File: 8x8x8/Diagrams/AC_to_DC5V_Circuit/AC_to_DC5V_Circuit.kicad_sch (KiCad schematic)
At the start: 30 parts, among them J1 Conn_01x01 (Arduino Signal Pi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, J10 Conn_01x01 (Q3 +5V), J11 Conn_01x01 (Q3 -5V), J12 Conn_01x01 (Q4 +5V), J13 Conn_01x01 (Q4 -5V), J2 Conn_01x03, J3 Conn_01x01 (Arduino ground), J4 Conn_01x03, J6 Conn_01x01 (Q1 +5V), J7 Conn_01x01 (Q1 -5V)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

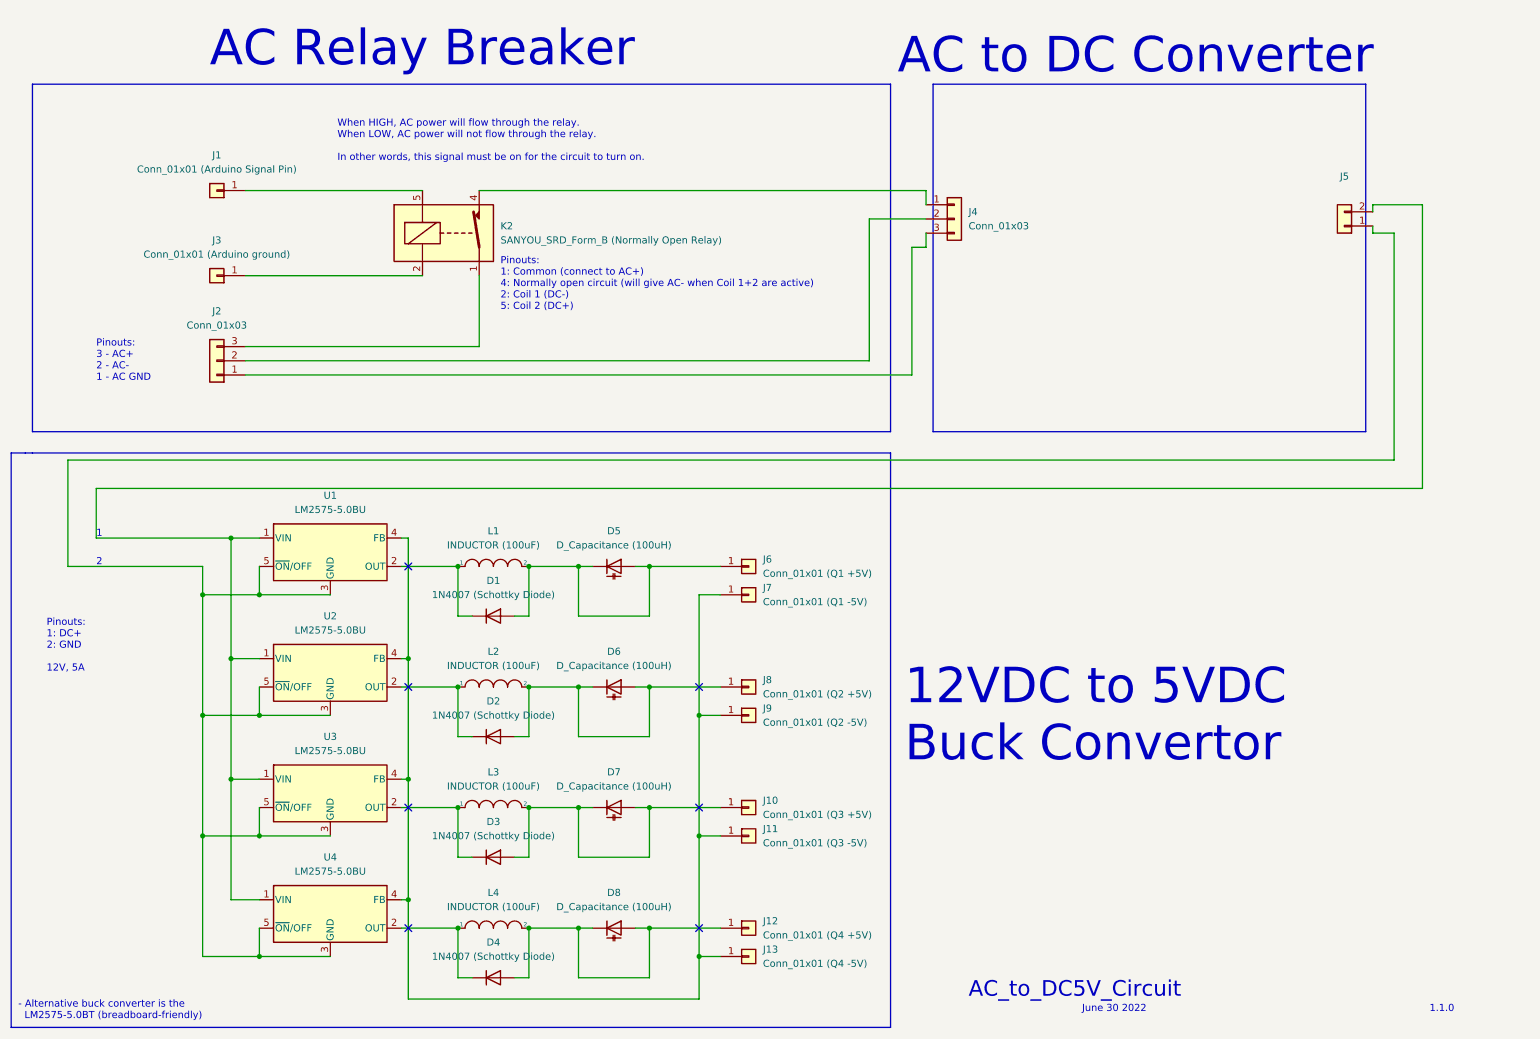
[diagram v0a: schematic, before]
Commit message: start AC->5VDC Circuit
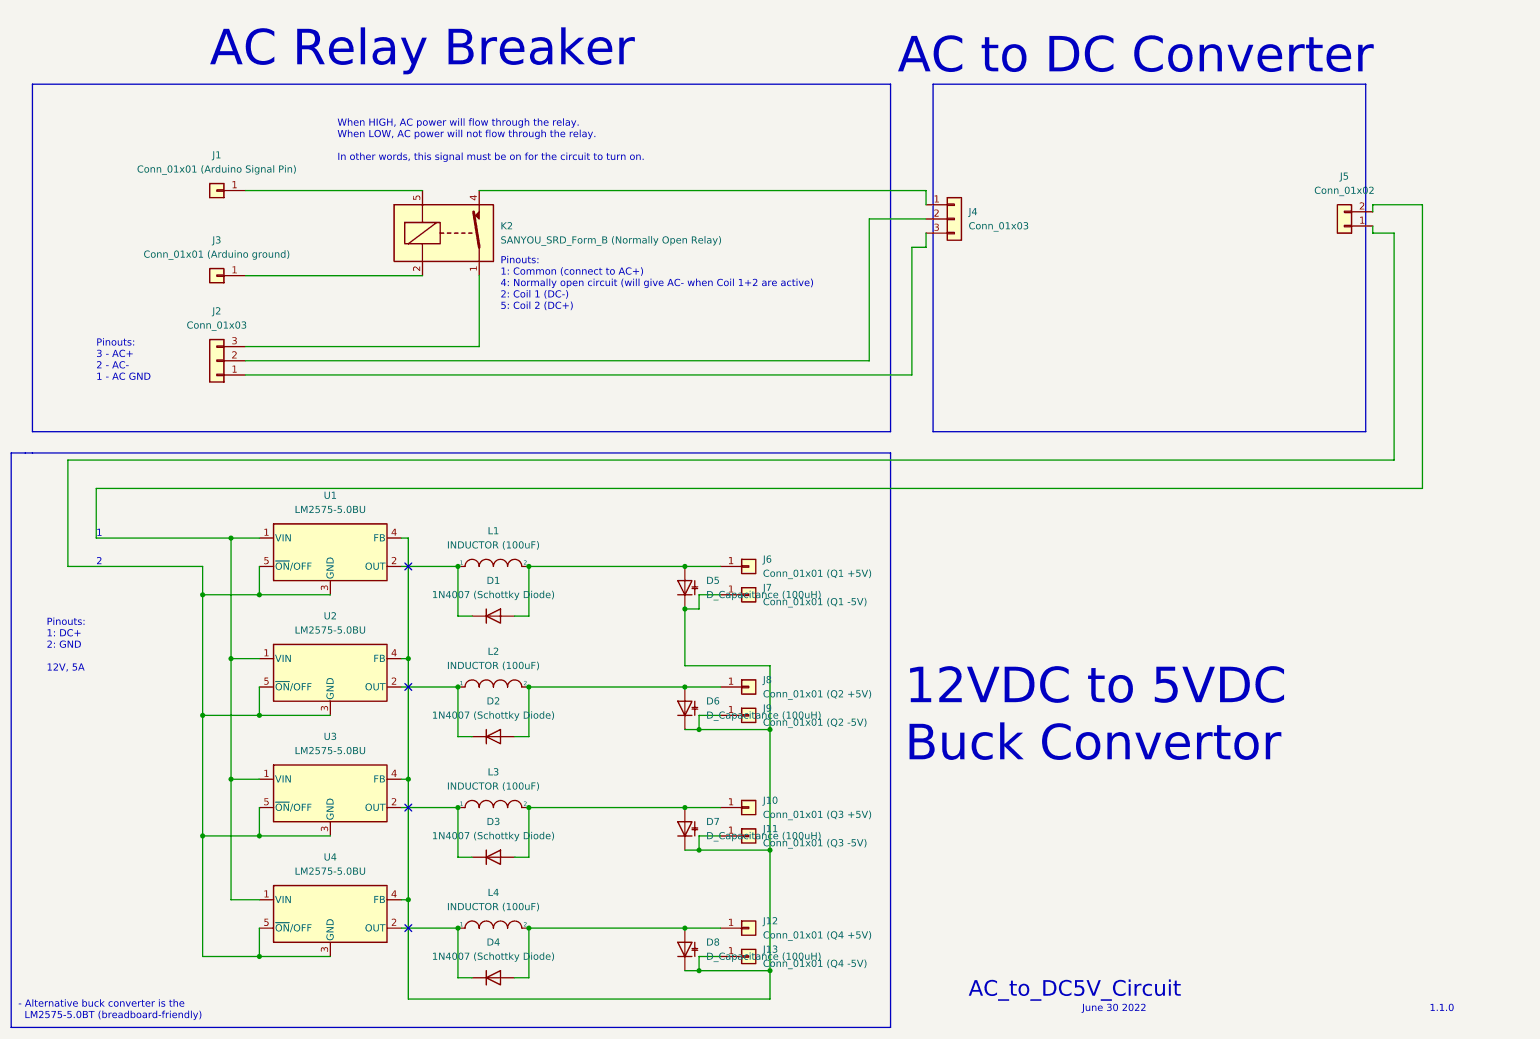
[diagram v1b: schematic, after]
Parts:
- J5: value (none) -> Conn_01x02; footprint (none) -> TerminalBlock_Phoenix:TerminalBlock_Phoenix_MKDS-1,5-2_1x02_P5.00mm_Horizontal
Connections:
- net at D2.2 (A), D6.2 (A), J8.1 (Pin_1)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: no longer D6.1 (K)
- net at D4.2 (A), D8.2 (A), J12.1 (Pin_1)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: no longer D8.1 (K)
- net at D1.2 (A), D5.2 (A), J6.1 (Pin_1)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: no longer D5.1 (K)
- net at J11.1 (Pin_1), J13.1 (Pin_1), J7.1 (Pin_1)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: now also D5.1 (K), D6.1 (K), D7.1 (K), D8.1 (K)
- net at D3.2 (A), D7.2 (A), J10.1 (Pin_1)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: no longer D7.1 (K)
- no-connect marks 7 -> 4
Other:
- moved on the sheet: D5, D6, D7, D8
